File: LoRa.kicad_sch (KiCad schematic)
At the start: 14 parts, among them IC8 317990687, J6 Conn_Coaxial, Q8 IRLML6402

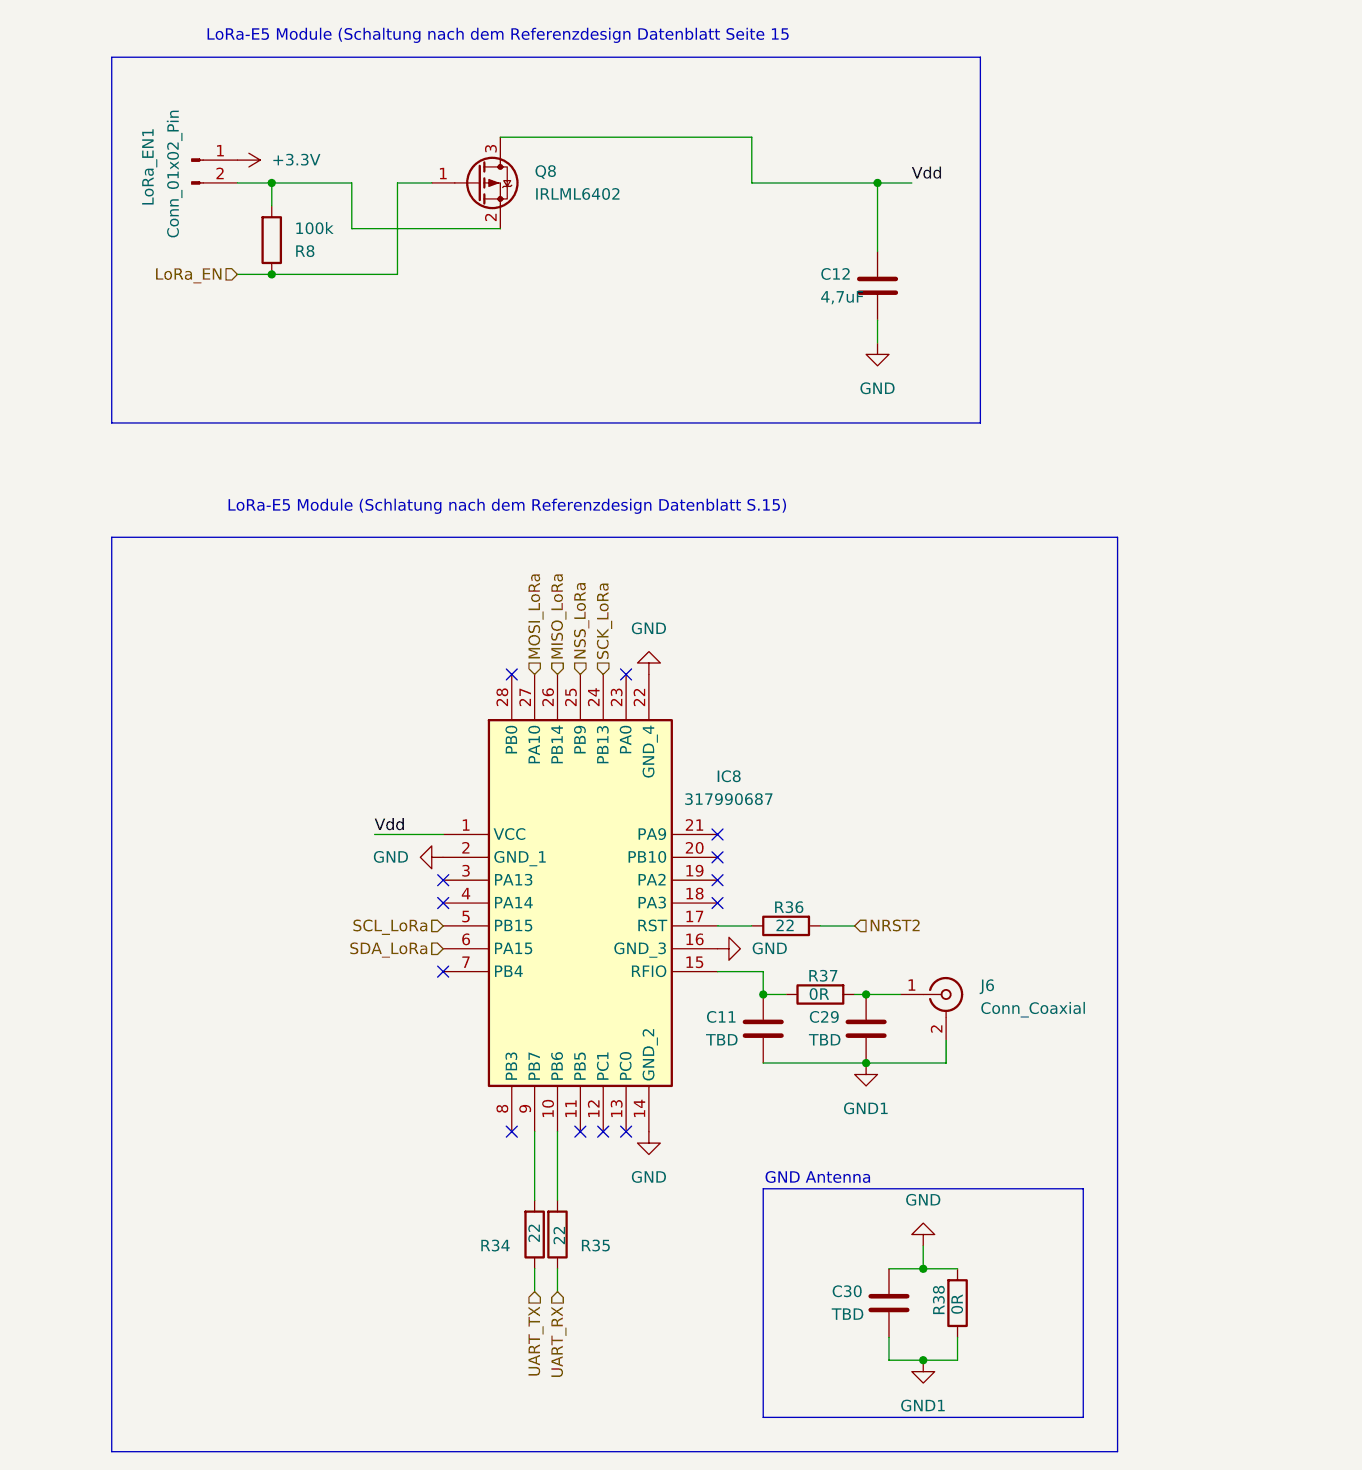
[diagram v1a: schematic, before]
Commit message: new layout
- recreation of the layout
- changed connection of ADC to MCU
- cleaner layout
- battery (supercap) for rtc
- crystal nearby the mcu
- 3V3 layer can be switched on/off separated from the mcu
- diode replaced with MOSFET
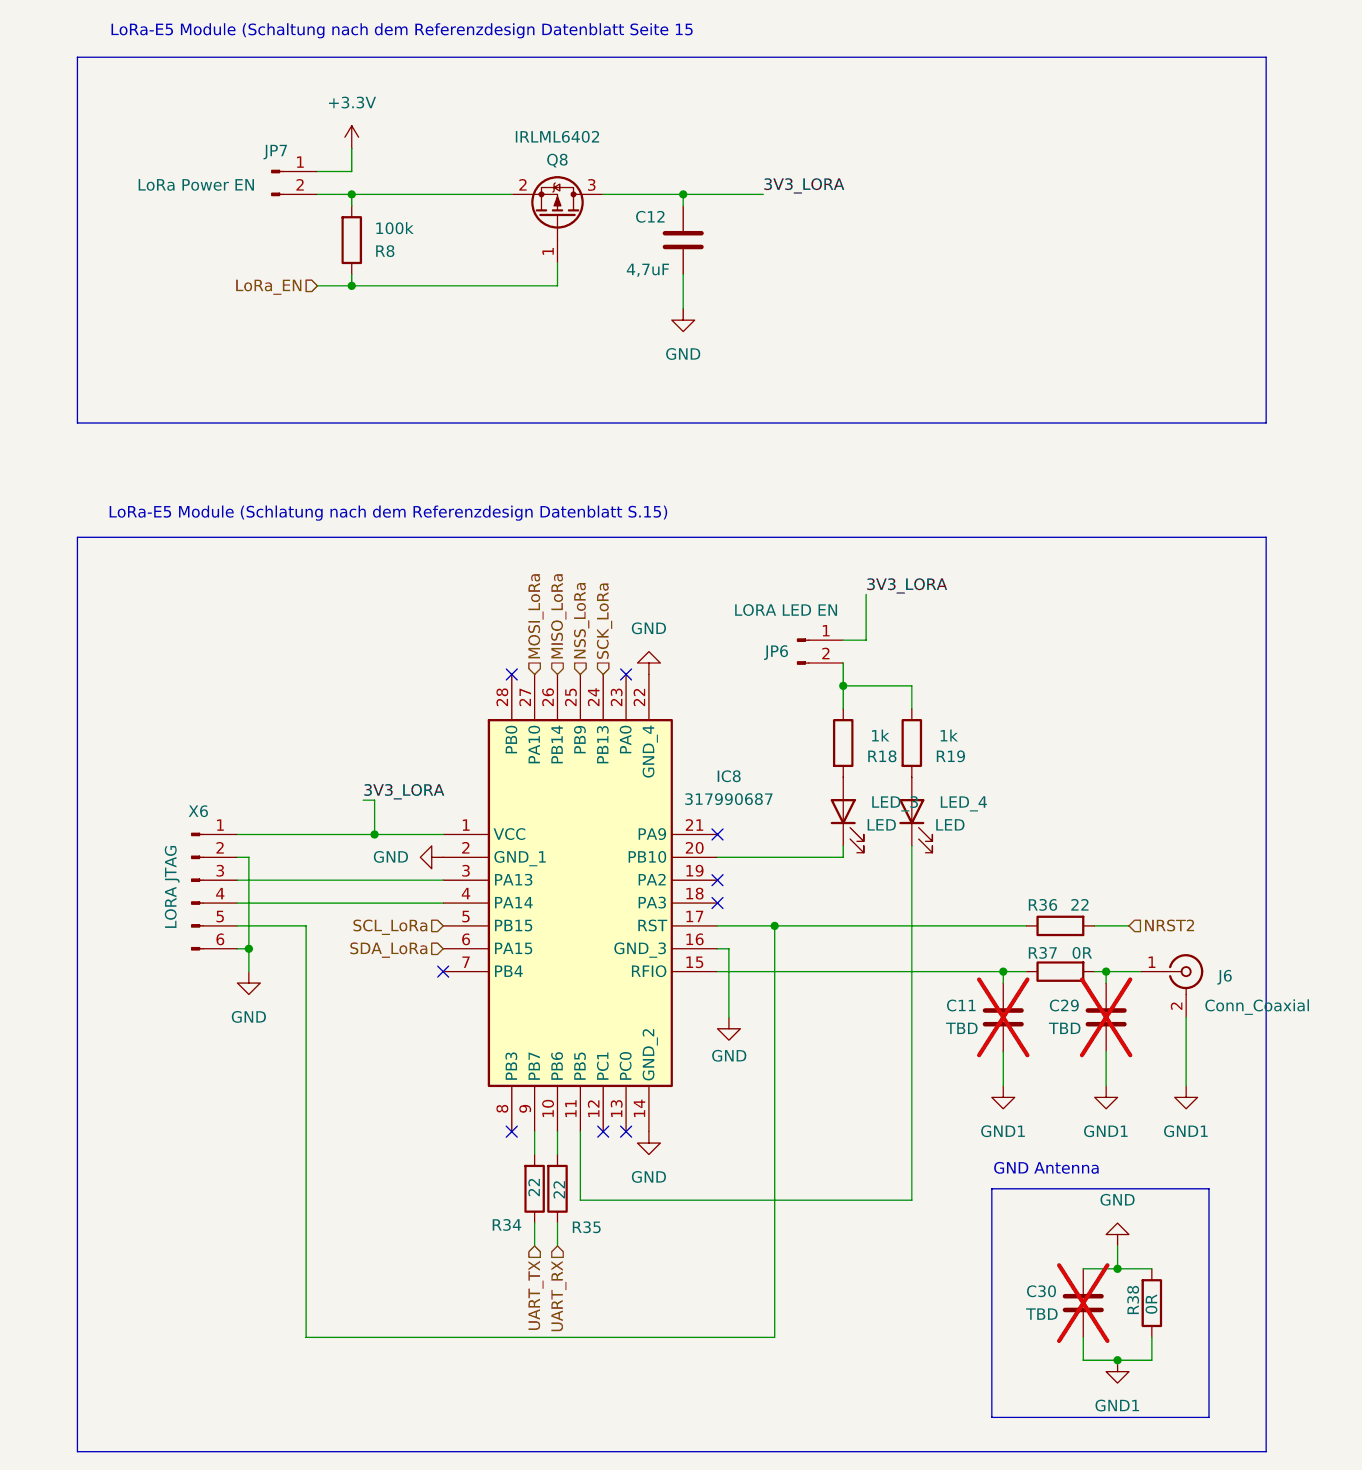
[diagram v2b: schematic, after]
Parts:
- added JP6: Conn_01x02_Pin, Connector_PinHeader_2.54mm:PinHeader_1x02_P2.54mm_Vertical, symbol Connector:Conn_01x02_Pin
- added LED_3, LED_4: LED, LED_SMD:LED_0805_2012Metric_Pad1.15x1.40mm_HandSolder, symbol Device:LED
- added R18, R19: 1k, Resistor_SMD:R_0805_2012Metric_Pad1.20x1.40mm_HandSolder, symbol Device:R
- added X6: Conn_01x06_Pin, Connector_PinHeader_2.54mm:PinHeader_1x06_P2.54mm_Vertical, symbol Connector:Conn_01x06_Pin
- C11, C29, C30: now not fitted
- JP7: renamed from LoRa_EN1; Mouser Part Number (none) -> 523-G800NA306018EU
- Q8: Mouser Part Number (none) -> 942-IRLML6402TRPBF
- R34, R35, R36: Mouser Part Number 660-RK73B2ATTE104J -> 594-MCU08050C2209FP5
- R37, R38: Mouser Part Number 660-RK73B2ATTE104J -> 279-CRG0805ZR
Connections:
- net GND: now also X6.2 (Pin_2), X6.6 (Pin_6)
- net at IC8.11 (PB5): now also LED_4.1 (K)
- net at IC8.17 (RST), R36.1: now also X6.5 (Pin_5)
- net at IC8.20 (PB10): now also LED_3.1 (K)
- net at IC8.3 (PA13): now also X6.3 (Pin_3)
- net at IC8.4 (PA14): now also X6.4 (Pin_4)
- net Vdd renamed 3V3_LORA
- net 3V3_LORA: now also JP6.1 (Pin_1), X6.1 (Pin_1)
- new net: JP6.2 (Pin_2), R18.1, R19.1
- new net: LED_4.2 (A), R19.2
- new net: LED_3.2 (A), R18.2
- no-connect marks 13 -> 9
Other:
- moved on the sheet: C12, J6, JP7, Q8, R34, R35, R36, R37, R38, R8
